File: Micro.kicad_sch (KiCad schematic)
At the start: 15 parts, among them J200 Conn_PIC_ICSP_ICD, J201 Conn_01x03_Male, Q200 Q_NPN_Darlington_CBE, Q201 Q_NPN_Darlington_CBE, U200 PIC16F1613-I/SL

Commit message: commit before starting kicad 7
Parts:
- C201: footprint (none) -> Capacitor_THT:CP_Radial_D25.0mm_P10.00mm_SnapIn
- R205: footprint (none) -> Resistor_SMD:R_0805_2012Metric_Pad1.20x1.40mm_HandSolder
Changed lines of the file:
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@@
       (effects (font (size 1.27 1.27)) (justify left))
     )
-    (property "Footprint" "" (id 2) (at 254 124.46 0)
+    (property "Footprint" "Resistor_SMD:R_0805_2012Metric_Pad1.20x1.40mm_HandSolder" (id 2) (at 254 124.46 0)
       (effects (font (size 1.27 1.27)) hide)
     )
@@
       (effects (font (size 1.27 1.27)) (justify left))
     )
-    (property "Footprint" "" (id 2) (at 254.9652 139.7 0)
-      (effects (font (size 1.27 1.27)) hide)
-    )
+    (property "Footprint" "Capacitor_THT:CP_Radial_D25.0mm_P10.00mm_SnapIn" (id 2) (at 254.9652 139.7 0)
+      (effects (font (size 1.27 1.27)) hide)
+    )

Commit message: move parts on the PCB
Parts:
- D200: value LED -> LED Yellow
- D201: value LED -> LED red
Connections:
- net Close: now reaches J201.1 (Pin_1), Q200.1 (C)
- net Open: now reaches J201.3 (Pin_3), Q201.1 (C)

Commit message: add test points, clean up errors
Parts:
- added TP4: 5019, AAA_Misc:KEYSTONE_5019, symbol AAA_Misc:5019
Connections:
- net BLP: now also TP4.TP
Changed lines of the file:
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@@
+    (stroke (width 0) (type default))
+  )
+  (wire (pts (xy 254 129.54) (xy 260.35 129.54))
     (stroke (width 0) (type default))
   )
@@
         )
       )
+    )
+  )
+  (symbol (lib_id "AAA_Misc:5019") (at 265.43 129.54 0) (unit 1)
+    (in_bom yes) (on_board yes) (dnp no) (fields_autoplaced)
+    (property "Reference" "TP4" (at 267.97 128.905 0)
+      (effects (font (size 1.27 1.27)) (justify left))
+    )
+    (property "Value" "5019" (at 267.97 131.445 0)
+      (effects (font (size 1.27 1.27)) (justify left))
+    )
+    (property "Footprint" "AAA_Misc:KEYSTONE_5019" (at 269.24 133.35 0)
+      (effects (font (size 1.27 1.27)) (justify left bottom) hide)
+    )
+    (property "Datasheet" "" (at 265.43 129.54 0)
+      (effects (font (size 1.27 1.27)) (justify left bottom) hide)
+    )
+    (property "PARTREV" "D" (at 265.43 129.54 0)
+      (effects (font (size 1.27 1.27)) (justify left bottom) hide)
+    )
+    (property "STANDARD" "Manufacturer Recommendations" (at 266.7 127 0)
+      (effects (font (size 1.27 1.27)) (justify left bottom) hide)
+    )
+    (property "MAXIMUM_PACKAGE_HEIGHT" "2.29 mm" (at 270.51 129.54 0)
+      (effects (font (size 1.27 1.27)) (justify left bottom) hide)
+    )
+    (property "MANUFACTURER" "Keystone Electronics" (at 266.7 125.73 0)
+      (effects (font (size 1.27 1.27)) (justify left bottom) hide)
+    )
+    (property "SNAPEDA_PN" "5019" (at 257.81 134.62 0)
+      (effects (font (size 1.27 1.27)) (justify left bottom) hide)
+    )
+    (pin "TP")
+    (instances
+      (project "2275Mod"
+        (path "/6ee24427-09ce-46d0-a3a3-2e623f3a3aa5/9ee275cc-47c1-4b8b-980c-7d7214ee4bde"
+          (reference "TP4") (unit 1)
+        )
+      )

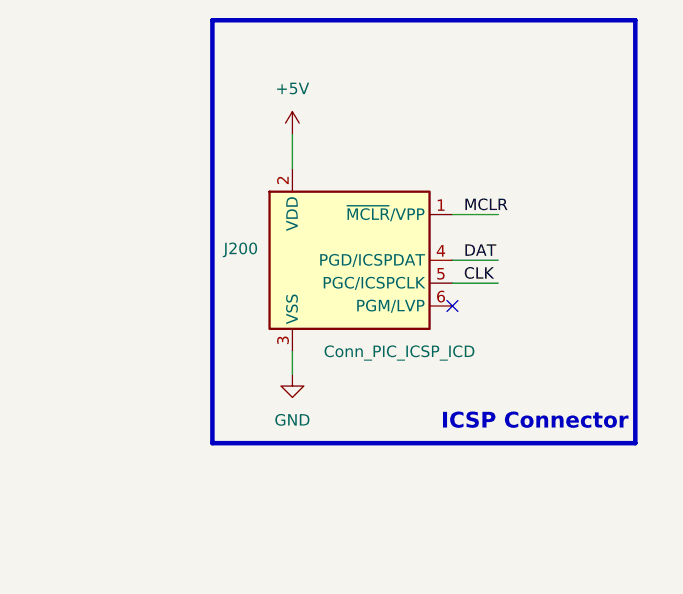
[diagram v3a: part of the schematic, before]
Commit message: make some traces thicker
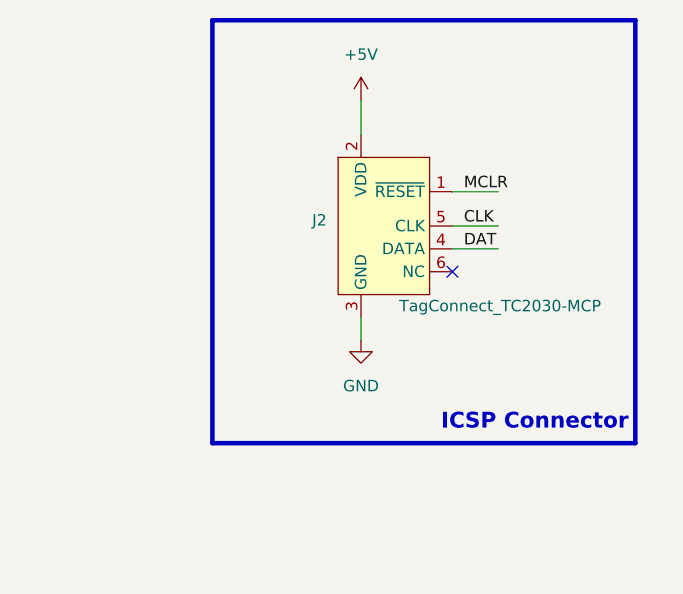
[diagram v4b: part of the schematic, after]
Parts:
- removed J200: Conn_PIC_ICSP_ICD, Connector_IDC:IDC-Header_2x03_P2.54mm_Vertical, symbol Connector:Conn_PIC_ICSP_ICD
- added J2: TagConnect_TC2030-MCP, Connector:Tag-Connect_TC2030-IDC-NL_2x03_P1.27mm_Vertical, symbol AAA_JH:TagConnect_TC2030-MCP
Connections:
- net +5V: now also J2.2 (VDD)
- net CLK: now also J2.5 (CLK)
- net DAT: now also J2.4 (DATA)
- net GND: now also J2.3 (GND)
- net MCLR: now also J2.1 (~{RESET})

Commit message: move traces, move c200 next to micro, genral clean up
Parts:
- D201: footprint LED_SMD:LED_0805_2012Metric_Pad1.15x1.40mm_HandSolder -> LED_SMD:LED_0603_1608Metric_Pad1.05x0.95mm_HandSolder
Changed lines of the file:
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@@
       (effects (font (size 1.27 1.27)))
     )
-    (property "Footprint" "LED_SMD:LED_0805_2012Metric_Pad1.15x1.40mm_HandSolder" (at 153.67 124.46 0)
+    (property "Footprint" "LED_SMD:LED_0603_1608Metric_Pad1.05x0.95mm_HandSolder" (at 153.67 124.46 0)
       (effects (font (size 1.27 1.27)) hide)
     )

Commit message: corrected q200 and q201 footprints
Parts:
- Q200, Q201: footprint AAA_JH:TRANS_2SD1918_ROM-M -> Package_TO_SOT_SMD:SOT-223-3_TabPin2
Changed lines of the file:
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@@
       (effects (font (size 1.27 1.27)) (justify left) hide)
     )
-    (property "Footprint" "AAA_JH:TRANS_2SD1918_ROM-M" (at 231.14 113.03 0)
+    (property "Footprint" "Package_TO_SOT_SMD:SOT-223-3_TabPin2" (at 231.14 113.03 0)
       (effects (font (size 1.27 1.27)) hide)
     )
@@
       (effects (font (size 1.27 1.27)) (justify left) hide)
     )
-    (property "Footprint" "AAA_JH:TRANS_2SD1918_ROM-M" (at 218.44 99.06 0)
+    (property "Footprint" "Package_TO_SOT_SMD:SOT-223-3_TabPin2" (at 218.44 99.06 0)
       (effects (font (size 1.27 1.27)) hide)
     )
